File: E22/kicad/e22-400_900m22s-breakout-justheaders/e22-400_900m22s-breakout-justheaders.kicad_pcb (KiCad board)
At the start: 2 copper layers, 24 x 27 mm, 5 parts, among them IC1 E22-900M22S, J1 Conn_01x07_Pin, J2 Conn_01x07_Pin

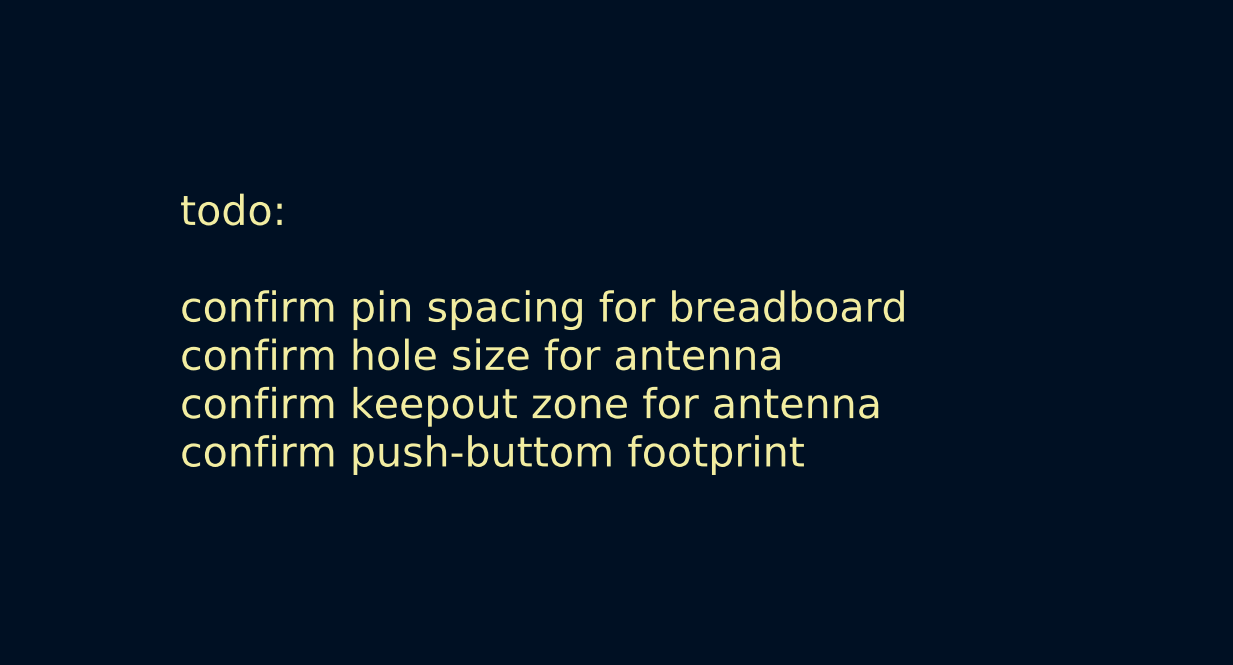
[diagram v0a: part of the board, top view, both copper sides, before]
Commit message: Created pdf of layout
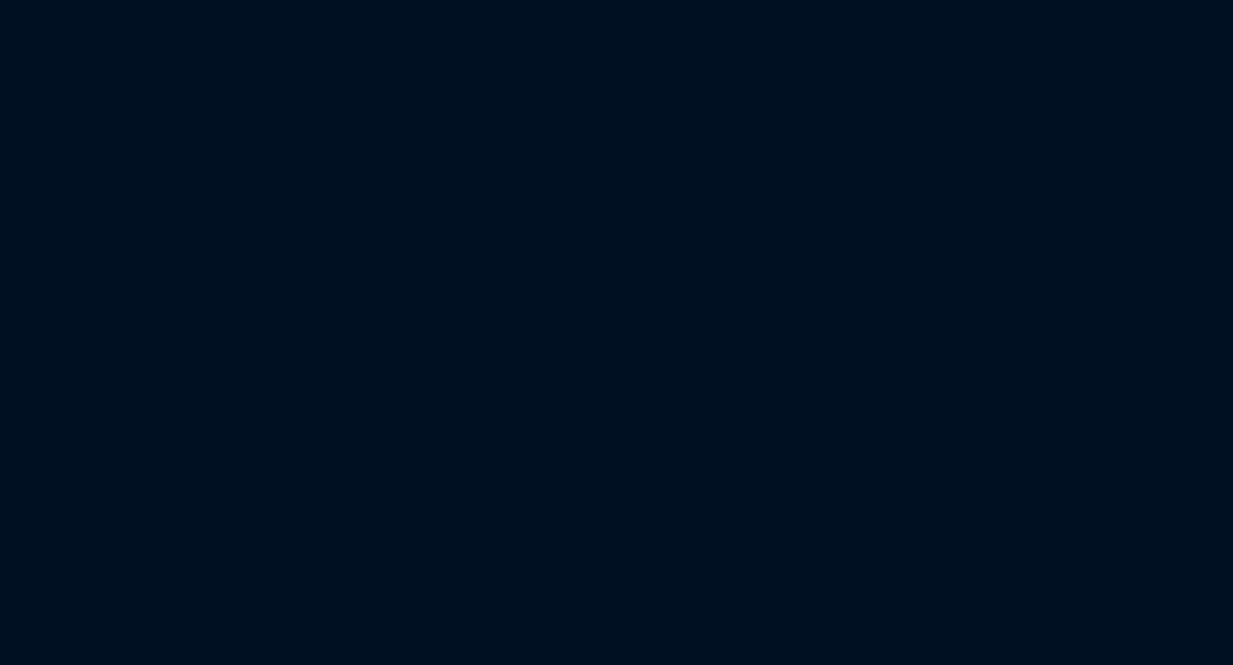
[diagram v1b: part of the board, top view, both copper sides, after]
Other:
- board text removed: "todo: confirm pin spacing for breadboard confirm hole size for antenna confirm keepout zone for antenna confirm push-buttom footprint"
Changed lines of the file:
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@@
-		)
-	)
-	(gr_text "todo:\n\nconfirm pin spacing for breadboard\nconfirm hole size for antenna\nconfirm keepout zone for antenna\nconfirm push-buttom footprint"
-		(at 175 115 0)
-		(layer "F.SilkS")
-		(effects
-			(font
-				(size 1 1)
-				(thickness 0.1)
-			)
-			(justify left bottom)
 		)
 	)
